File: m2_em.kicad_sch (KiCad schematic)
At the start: 25 parts, among them J94 Bus_M.2_Socket_M, J95 Bus_M.2_Socket_E

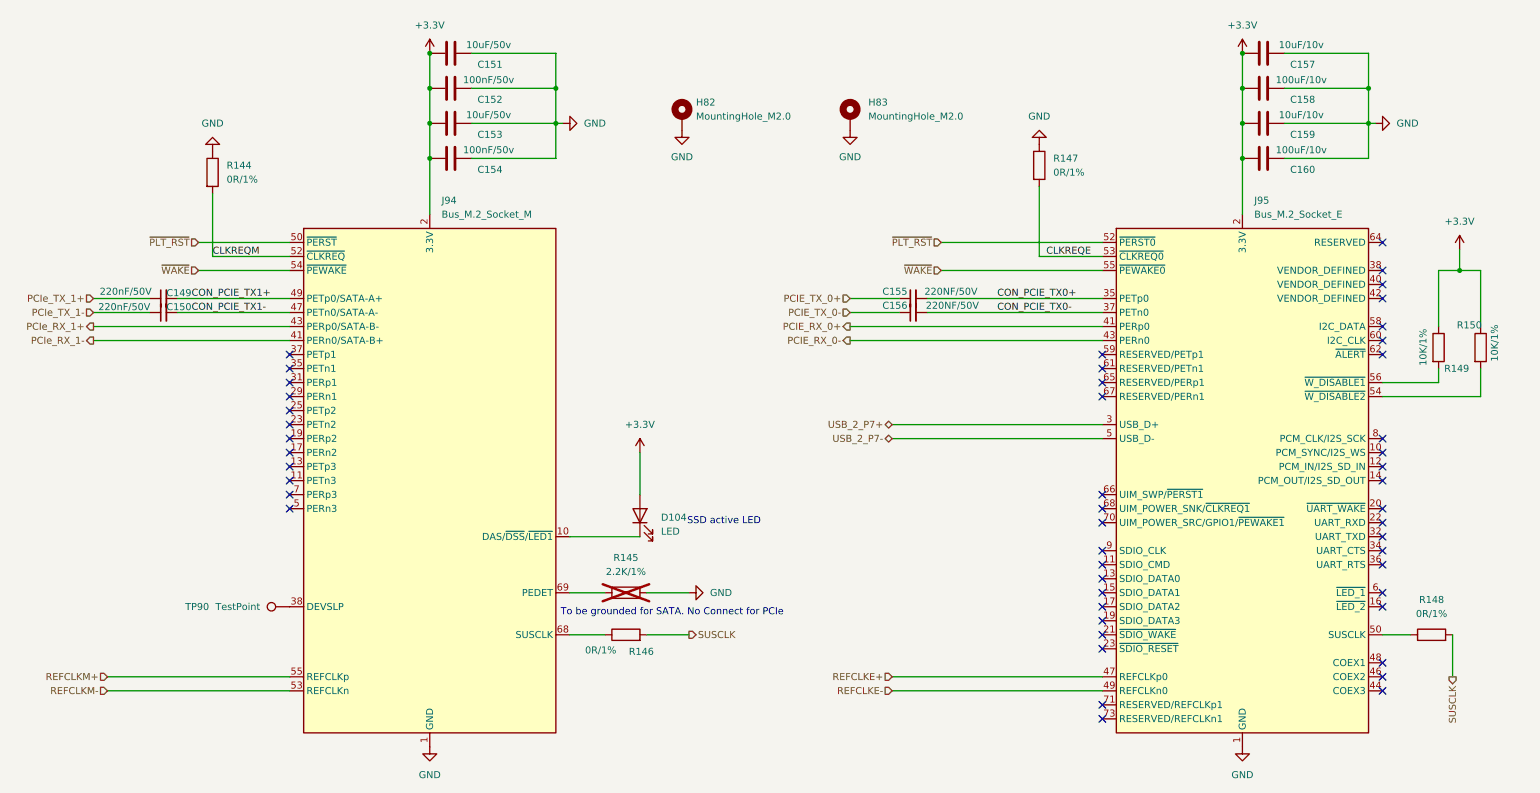
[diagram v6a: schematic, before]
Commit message: Designators in M.2 restored
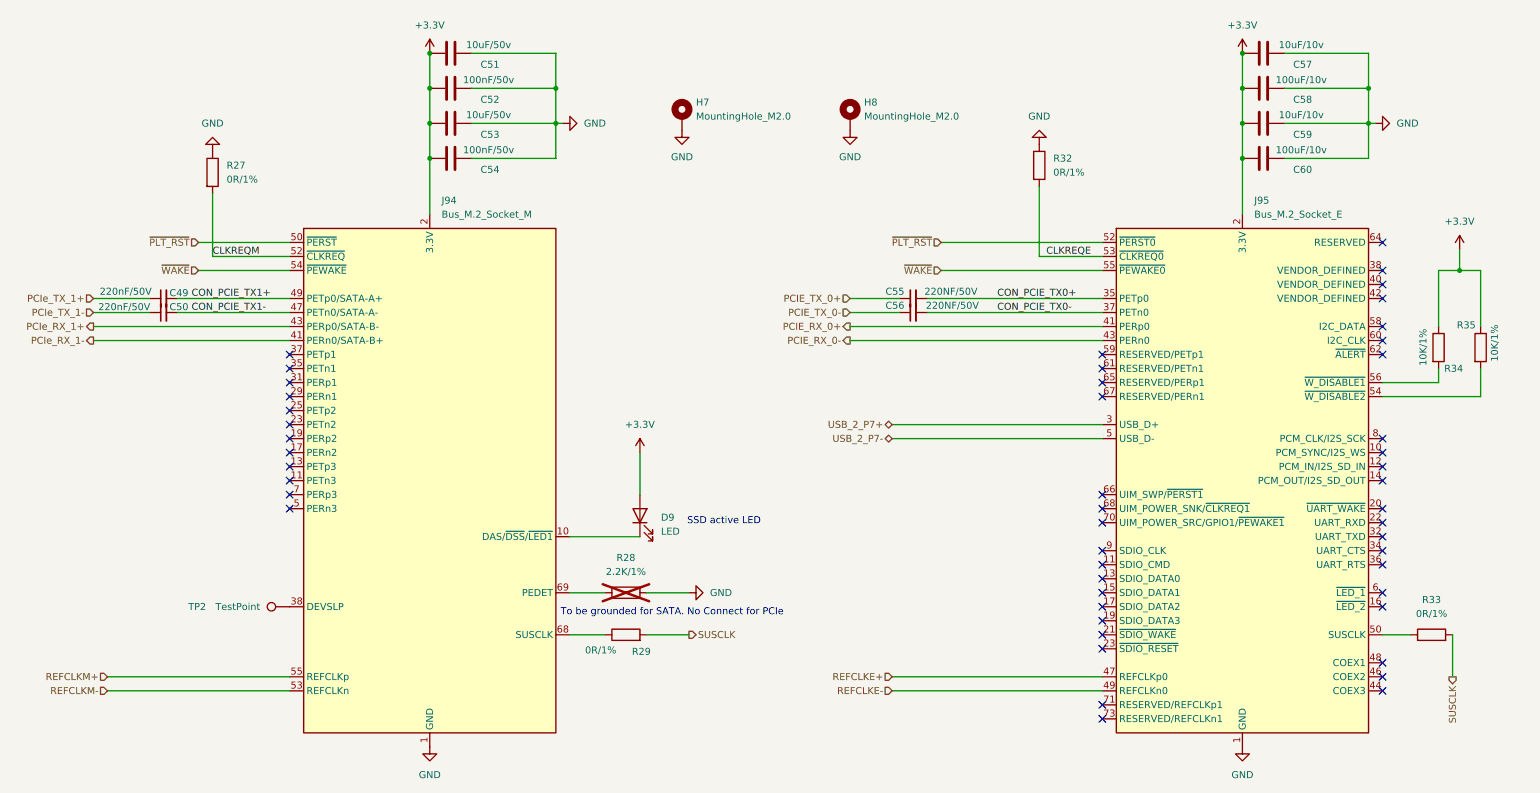
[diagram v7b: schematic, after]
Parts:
- renumbered C149 to C49, C150 to C50, C151 to C51, C152 to C52, C153 to C53, C154 to C54, C155 to C55, C156 to C56, C157 to C57, C158 to C58, C159 to C59, C160 to C60, D104 to D9, H82 to H7, H83 to H8, R144 to R27, R145 to R28, R146 to R29, R147 to R32, R148 to R33, R149 to R34, R150 to R35, TP90 to TP2
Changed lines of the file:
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@@
 		(in_pos_files yes)
 		(dnp no)
-		(property "Reference" "C150"
+		(property "Reference" "C50"
 			(at 40.894 76.454 90)
 			(show_name no)
@@
 			(project "Carrier_Board"
 				(path "/e768274e-12f3-4f83-96f6-abb7638e0bc1/c9d591b5-2734-4735-842a-ee158b52d7b9"
-					(reference "C150")
+					(reference "C50")
 					(unit 1)
 				)
@@
 		(dnp no)
 		(fields_autoplaced yes)
-		(property "Reference" "H83"
-			(at 165.862 39.3699 0)
+		(property "Reference" "H8"
+			(at 165.1 39.3699 0)
 			(show_name no)
 			(do_not_autoplace no)
@@
 		)
 		(property "Value" "MountingHole_M2.0"
-			(at 165.862 41.9099 0)
+			(at 165.1 41.9099 0)
 			(show_name no)
 			(do_not_autoplace no)
@@
 			(project "Carrier_Board"
 				(path "/e768274e-12f3-4f83-96f6-abb7638e0bc1/c9d591b5-2734-4735-842a-ee158b52d7b9"
-					(reference "H83")
+					(reference "H8")
 					(unit 1)
 				)
@@
 		(in_pos_files yes)
 		(dnp no)
-		(property "Reference" "R150"
+		(property "Reference" "R35"
 			(at 272.542 79.756 0)
 			(show_name no)
@@
 			(project "Carrier_Board"
 				(path "/e768274e-12f3-4f83-96f6-abb7638e0bc1/c9d591b5-2734-4735-842a-ee158b52d7b9"
-					(reference "R150")
+					(reference "R35")
 					(unit 1)
 				)
@@
 		(dnp yes)
 		(fields_autoplaced yes)
-		(property "Reference" "R145"
+		(property "Reference" "R28"
 			(at 121.92 121.92 90)
 			(show_name no)
@@
 			(project "Carrier_Board"
 				(path "/e768274e-12f3-4f83-96f6-abb7638e0bc1/c9d591b5-2734-4735-842a-ee158b52d7b9"
-					(reference "R145")
+					(reference "R28")
 					(unit 1)
 				)
@@
 		(in_pos_files yes)
 		(dnp no)
-		(property "Reference" "C159"
+		(property "Reference" "C59"
 			(at 244.602 45.212 90)
 			(show_name no)
@@
 			(project "Carrier_Board"
 				(path "/e768274e-12f3-4f83-96f6-abb7638e0bc1/c9d591b5-2734-4735-842a-ee158b52d7b9"
-					(reference "C159")
+					(reference "C59")
 					(unit 1)
 				)
@@
 		(in_pos_files yes)
 		(dnp no)
-		(property "Reference" "C152"
+		(property "Reference" "C52"
 			(at 97.282 38.862 90)
 			(show_name no)
@@
 			(project "Carrier_Board"
 				(path "/e768274e-12f3-4f83-96f6-abb7638e0bc1/c9d591b5-2734-4735-842a-ee158b52d7b9"
-					(reference "C152")
+					(reference "C52")
 					(unit 1)
 				)
@@
 		(in_pos_files yes)
 		(dnp no)
-		(property "Reference" "R149"
+		(property "Reference" "R34"
 			(at 270.256 87.63 0)
 			(show_name no)
@@
 			(project "Carrier_Board"
 				(path "/e768274e-12f3-4f83-96f6-abb7638e0bc1/c9d591b5-2734-4735-842a-ee158b52d7b9"
-					(reference "R149")
+					(reference "R34")
 					(unit 1)
 				)
@@
 		(dnp no)
 		(fields_autoplaced yes)
-		(property "Reference" "R148"
+		(property "Reference" "R33"
 			(at 267.97 129.54 90)
 			(show_name no)
@@
 			(project "Carrier_Board"
 				(path "/e768274e-12f3-4f83-96f6-abb7638e0bc1/c9d591b5-2734-4735-842a-ee158b52d7b9"
-					(reference "R148")
+					(reference "R33")
 					(unit 1)
 				)
@@
 		(in_pos_files yes)
 		(dnp no)
-		(property "Reference" "C156"
+		(property "Reference" "C56"
 			(at 170.688 76.2 90)
 			(show_name no)
@@
 			(project "Carrier_Board"
 				(path "/e768274e-12f3-4f83-96f6-abb7638e0bc1/c9d591b5-2734-4735-842a-ee158b52d7b9"
-					(reference "C156")
+					(reference "C56")
 					(unit 1)
 				)
@@
 		(in_pos_files yes)
 		(dnp no)
-		(property "Reference" "C154"
+		(property "Reference" "C54"
 			(at 97.282 51.562 90)
 			(show_name no)
@@
 			(project "Carrier_Board"
 				(path "/e768274e-12f3-4f83-96f6-abb7638e0bc1/c9d591b5-2734-4735-842a-ee158b52d7b9"
-					(reference "C154")
+					(reference "C54")
 					(unit 1)
 				)
@@
 		(in_pos_files yes)
 		(dnp no)
-		(property "Reference" "C153"
+		(property "Reference" "C53"
 			(at 97.282 45.212 90)
 			(show_name no)
@@
 			(project "Carrier_Board"
 				(path "/e768274e-12f3-4f83-96f6-abb7638e0bc1/c9d591b5-2734-4735-842a-ee158b52d7b9"
-					(reference "C153")
+					(reference "C53")
 					(unit 1)
 				)
@@
 		(in_pos_files yes)
 		(dnp no)
-		(property "Reference" "TP90"
+		(property "Reference" "TP2"
 			(at 44.196 130.81 90)
 			(show_name no)
@@
 			(project "Carrier_Board"
 				(path "/e768274e-12f3-4f83-96f6-abb7638e0bc1/c9d591b5-2734-4735-842a-ee158b52d7b9"
-					(reference "TP90")
+					(reference "TP2")
 					(unit 1)
 				)
@@
 		(in_pos_files yes)
 		(dnp no)
-		(property "Reference" "R146"
+		(property "Reference" "R29"
 			(at 124.714 138.938 90)
 			(show_name no)
@@
 			(project "Carrier_Board"
 				(path "/e768274e-12f3-4f83-96f6-abb7638e0bc1/c9d591b5-2734-4735-842a-ee158b52d7b9"
-					(reference "R146")
+					(reference "R29")
 					(unit 1)
 				)
@@
 		(in_pos_files yes)
 		(dnp no)
-		(property "Reference" "C151"
+		(property "Reference" "C51"
 			(at 97.282 32.512 90)
 			(show_name no)
@@
 			(project "Carrier_Board"
 				(path "/e768274e-12f3-4f83-96f6-abb7638e0bc1/c9d591b5-2734-4735-842a-ee158b52d7b9"
-					(reference "C151")
+					(reference "C51")
 					(unit 1)
 				)
@@
 		(in_pos_files yes)
 		(dnp no)
-		(property "Reference" "C160"
+		(property "Reference" "C60"
 			(at 244.602 51.562 90)
 			(show_name no)
@@
 			(project "Carrier_Board"
 				(path "/e768274e-12f3-4f83-96f6-abb7638e0bc1/c9d591b5-2734-4735-842a-ee158b52d7b9"
-					(reference "C160")
+					(reference "C60")
 					(unit 1)
 				)
@@
 		(in_pos_files yes)
 		(dnp no)
-		(property "Reference" "C155"
+		(property "Reference" "C55"
 			(at 170.688 73.66 90)
 			(show_name no)
@@
 			(project "Carrier_Board"
 				(path "/e768274e-12f3-4f83-96f6-abb7638e0bc1/c9d591b5-2734-4735-842a-ee158b52d7b9"
-					(reference "C155")
+					(reference "C55")
 					(unit 1)
 				)
@@
 		(dnp no)
 		(fields_autoplaced yes)
-		(property "Reference" "H82"
+		(property "Reference" "H7"
 			(at 134.62 39.3699 0)
 			(show_name no)
@@
 			(project "Carrier_Board"
 				(path "/e768274e-12f3-4f83-96f6-abb7638e0bc1/c9d591b5-2734-4735-842a-ee158b52d7b9"
-					(reference "H82")
+					(reference "H7")
 					(unit 1)
 				)
@@
 		(in_pos_files yes)
 		(dnp no)
-		(property "Reference" "C158"
+		(property "Reference" "C58"
 			(at 244.602 38.862 90)
 			(show_name no)
@@
 			(project "Carrier_Board"
 				(path "/e768274e-12f3-4f83-96f6-abb7638e0bc1/c9d591b5-2734-4735-842a-ee158b52d7b9"
-					(reference "C158")
+					(reference "C58")
 					(unit 1)
 				)
@@
 		(in_pos_files yes)
 		(dnp no)
-		(property "Reference" "C149"
+		(property "Reference" "C49"
 			(at 40.894 73.914 90)
 			(show_name no)
@@
 			(project "Carrier_Board"
 				(path "/e768274e-12f3-4f83-96f6-abb7638e0bc1/c9d591b5-2734-4735-842a-ee158b52d7b9"
-					(reference "C149")
+					(reference "C49")
 					(unit 1)
 				)
@@
 		(dnp no)
 		(fields_autoplaced yes)
-		(property "Reference" "R147"
+		(property "Reference" "R32"
 			(at 199.39 49.5299 0)
 			(show_name no)
@@
 			(project "Carrier_Board"
 				(path "/e768274e-12f3-4f83-96f6-abb7638e0bc1/c9d591b5-2734-4735-842a-ee158b52d7b9"
-					(reference "R147")
+					(reference "R32")
 					(unit 1)
 				)
@@
 		(dnp no)
 		(fields_autoplaced yes)
-		(property "Reference" "D104"
+		(property "Reference" "D9"
 			(at 128.27 114.6174 90)
 			(show_name no)
@@
 			(project "Carrier_Board"
 				(path "/e768274e-12f3-4f83-96f6-abb7638e0bc1/c9d591b5-2734-4735-842a-ee158b52d7b9"
-					(reference "D104")
+					(reference "D9")
 					(unit 1)
 				)
@@
 		(in_pos_files yes)
 		(dnp no)
-		(property "Reference" "C157"
+		(property "Reference" "C57"
 			(at 244.602 32.512 90)
 			(show_name no)
@@
 			(project "Carrier_Board"
 				(path "/e768274e-12f3-4f83-96f6-abb7638e0bc1/c9d591b5-2734-4735-842a-ee158b52d7b9"
-					(reference "C157")
+					(reference "C57")
 					(unit 1)
 				)
@@
 		(dnp no)
 		(fields_autoplaced yes)
-		(property "Reference" "R144"
+		(property "Reference" "R27"
 			(at 49.53 50.7999 0)
 			(show_name no)
@@
 			(project "Carrier_Board"
 				(path "/e768274e-12f3-4f83-96f6-abb7638e0bc1/c9d591b5-2734-4735-842a-ee158b52d7b9"
-					(reference "R144")
+					(reference "R27")
 					(unit 1)
 				)

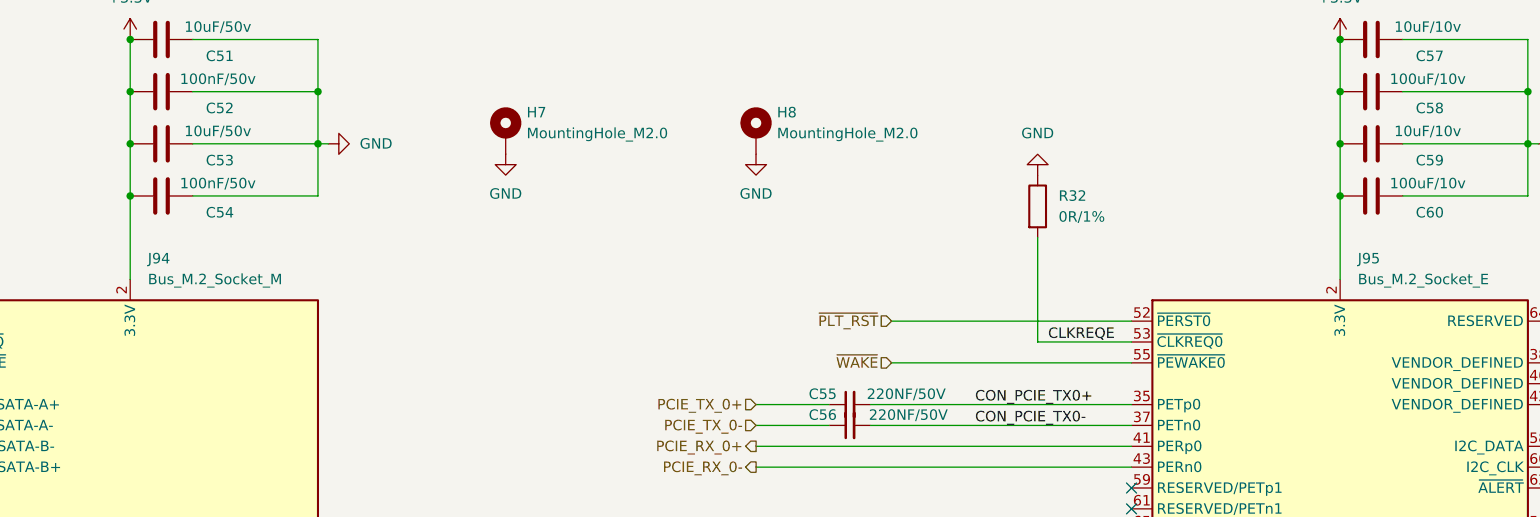
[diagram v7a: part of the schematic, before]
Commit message: Designators in PSU restored
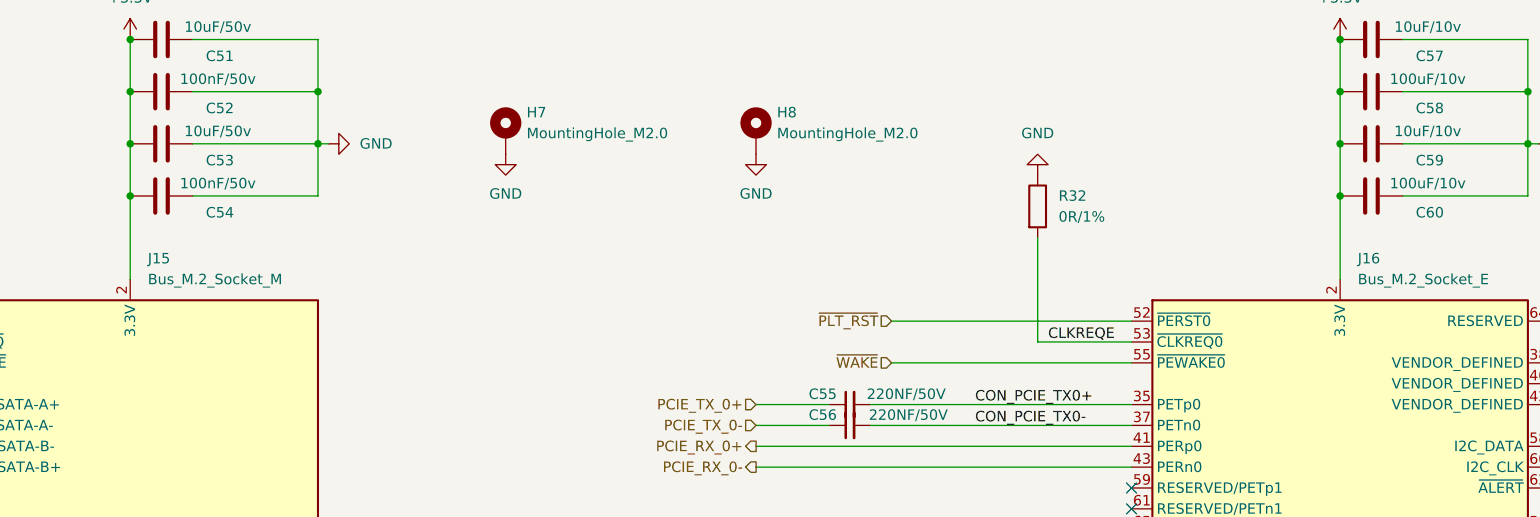
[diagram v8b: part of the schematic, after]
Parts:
- renumbered J94 to J15, J95 to J16
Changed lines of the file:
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@@
 		(dnp no)
 		(fields_autoplaced yes)
-		(property "Reference" "J94"
+		(property "Reference" "J15"
 			(at 88.5033 57.15 0)
 			(show_name no)
@@
 			(project "Carrier_Board"
 				(path "/e768274e-12f3-4f83-96f6-abb7638e0bc1/c9d591b5-2734-4735-842a-ee158b52d7b9"
-					(reference "J94")
+					(reference "J15")
 					(unit 1)
 				)
@@
 		(dnp no)
 		(fields_autoplaced yes)
-		(property "Reference" "J95"
+		(property "Reference" "J16"
 			(at 235.8233 57.15 0)
 			(show_name no)
@@
 			(project "Carrier_Board"
 				(path "/e768274e-12f3-4f83-96f6-abb7638e0bc1/c9d591b5-2734-4735-842a-ee158b52d7b9"
-					(reference "J95")
+					(reference "J16")
 					(unit 1)
 				)
